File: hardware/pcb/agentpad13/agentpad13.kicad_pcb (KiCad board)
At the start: 2 copper layers, 84.2 x 100 mm, 126 parts, among them J1 USB-C, J2 EXPANSION, SW1 MX_Hotswap, SW10 MX_Hotswap, SW11 MX_Hotswap, SW12 MX_Hotswap, SW13 MX_Hotswap, SW14 BOOT, SW15 RESET, SW2 MX_Hotswap, SW3 MX_Hotswap, SW4 MX_Hotswap, SW5 MX_Hotswap, SW6 MX_Hotswap, SW7 MX_Hotswap, SW8 MX_Hotswap, SW9 MX_Hotswap, U1 RP2040, U2 W25Q128JVSIQ, U3 AP2112K-3.3, U4 USBLC6-2SC6, U5 SN74LVC1T45, U6 TTP223, Y1 12MHz ABM8-272-T3

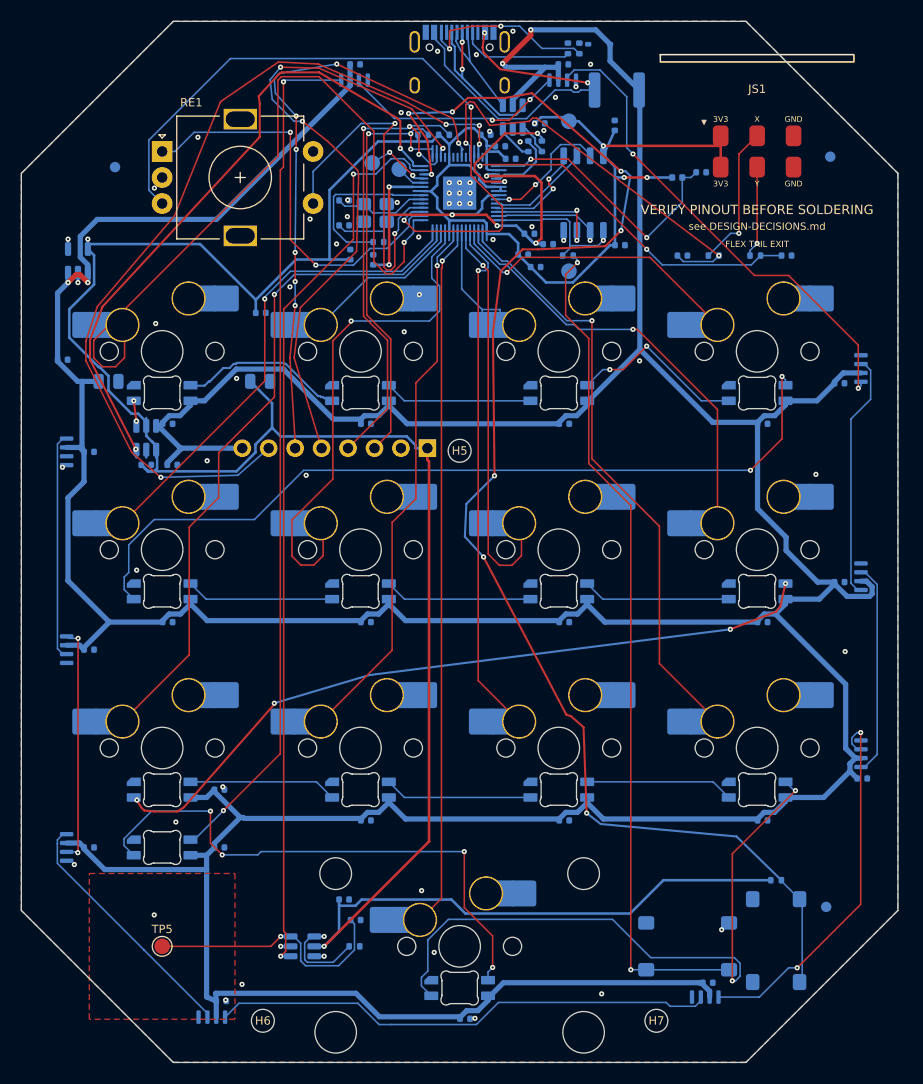
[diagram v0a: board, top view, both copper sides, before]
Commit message: v5: corrected board (encoder/USB-C/joystick), case v2.5 + toppers + gasket, ordering guide
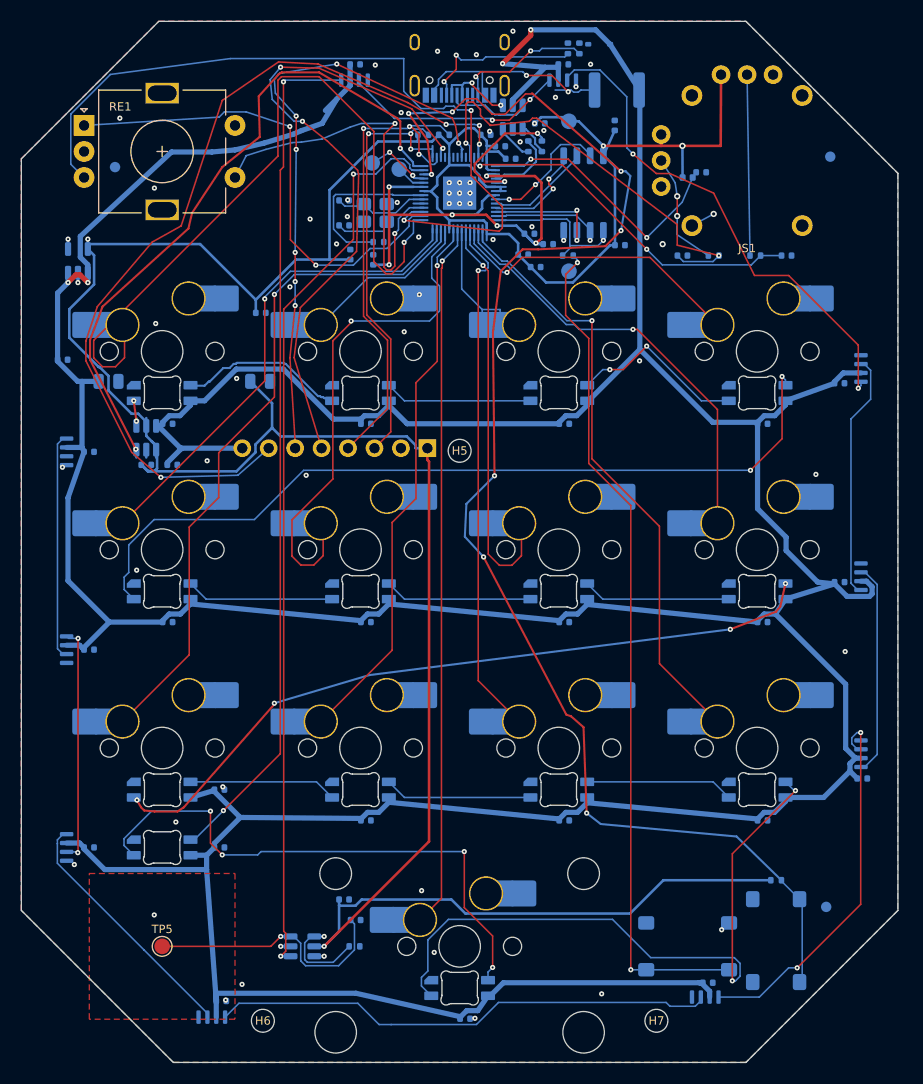
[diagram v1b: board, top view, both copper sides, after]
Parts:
- JS1: value PSP-Slider -> YA13-FL7.4-B5Ka; footprint JS1_PSP_slider_4pad_handsolder -> Joystick:YA13-FL7.4-B5Ka_C37323742
- moved RE1 7.91 mm to (6.03, 10.0)
- moved J1 2.05 mm to (42.1, 3.05), turned to 0 degrees
- moved JS1 1.30 mm to (69.7, 13.4), turned to 180 degrees
- moved FB1 1.00 mm to (64.0, 15.0)
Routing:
- net VBUS: track 35.0 -> 22.0 mm
- net JOY_Y: track 8.78 -> 17.4 mm, vias 1 -> 0
- net PORT_DP: track 16.9 -> 9.06 mm, vias 2 -> 0
- net ENC_A: track 39.6 -> 47.3 mm
- net ENC_B: track 67.9 -> 75.3 mm
- net +5V: track 519.8 -> 514.3 mm
- net CC1: track 10.9 -> 15.6 mm, vias 0 -> 2
- net ENC_SW: track 36.0 -> 40.3 mm
- net CC2: track 17.3 -> 13.1 mm
- net PORT_DM: track 11.3 -> 7.95 mm, vias 0 -> 2
- net JOY_X: track 13.9 -> 11.1 mm, vias 1 -> 2
- net GND: track 5.55 -> 7.92 mm, vias 56 -> 59
- net RUN: track 138.7 -> 140.2 mm
- net JOY_X_ADC: track 39.9 -> 41.2 mm
- net RGB_D16: track 47.2 -> 48.4 mm
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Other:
- outline, holes or cut-outs redrawn

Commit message: Board: the bottom two underglow LEDs were firing out of the case, not into it
Six of the ten underglow LEDs point inward and diffuse through the band.
Four pointed outward and read as visible dots instead of a glow. Found on
an assembled board.

Not an assembly fault. These are daisy-chained SK6812-SIDE parts, so a
180-degree misplacement would reverse VDD/VSS and DIN/DOUT and kill that
LED plus everything downstream of it. All ten light. The fab placed
exactly what the files said.

The generator declared a coherent all-inward rotation set, then applied
the rotation and only afterwards flipped each part to the back copper.
That flip negates orientation, so the two LEDs firing along Y reversed
while the six firing along X survived. The left and right rails were
right all along.

This rotates the two LEDs on the far edge from the USB connector. The two
beside the connector stay outward on purpose -- the accent there is
wanted. Result: eight inward, two outward by choice.

Only those two footprints move, and only their rotation: 126 footprints
compared, 414 pads with zero net changes, copper touched on just the four
nets those LEDs connect to, four vias added and none removed. The LED
chain order is unchanged, so firmware needs no update.

Gates: DRC 0, unconnected 0, contract 45/45, +5V spine min 0.5 mm, USB
pair clean, touch pour unchanged, fabpack verify 31/31.

The first units were built from the previous revision and cannot be
corrected -- rotating a part means moving its pads, so it needs a respin.
This is the corrected design for anyone building the board from here.
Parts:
- turned LED20 to 180 degrees
- turned LED21 to 180 degrees
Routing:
- net RGB_D20: track 48.7 -> 60.1 mm
- net RGB_D21: track 24.1 -> 29.2 mm, vias 0 -> 2
- net RGB_D19: track 36.6 -> 40.4 mm, vias 2 -> 4
- net +5V: track 514.3 -> 516.7 mm
